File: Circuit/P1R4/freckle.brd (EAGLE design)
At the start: 57.9 x 57.9 mm, 81 parts, among them J1 1981584-1, U1 MK20DX256VLH7, U2 TPS61200, U3 MPU-9250, U4 MINI54TAN, Y1 32.768KHz, Y2 16Mhz/8pF, Y3 26 Mhz, Y4 16 Mhz

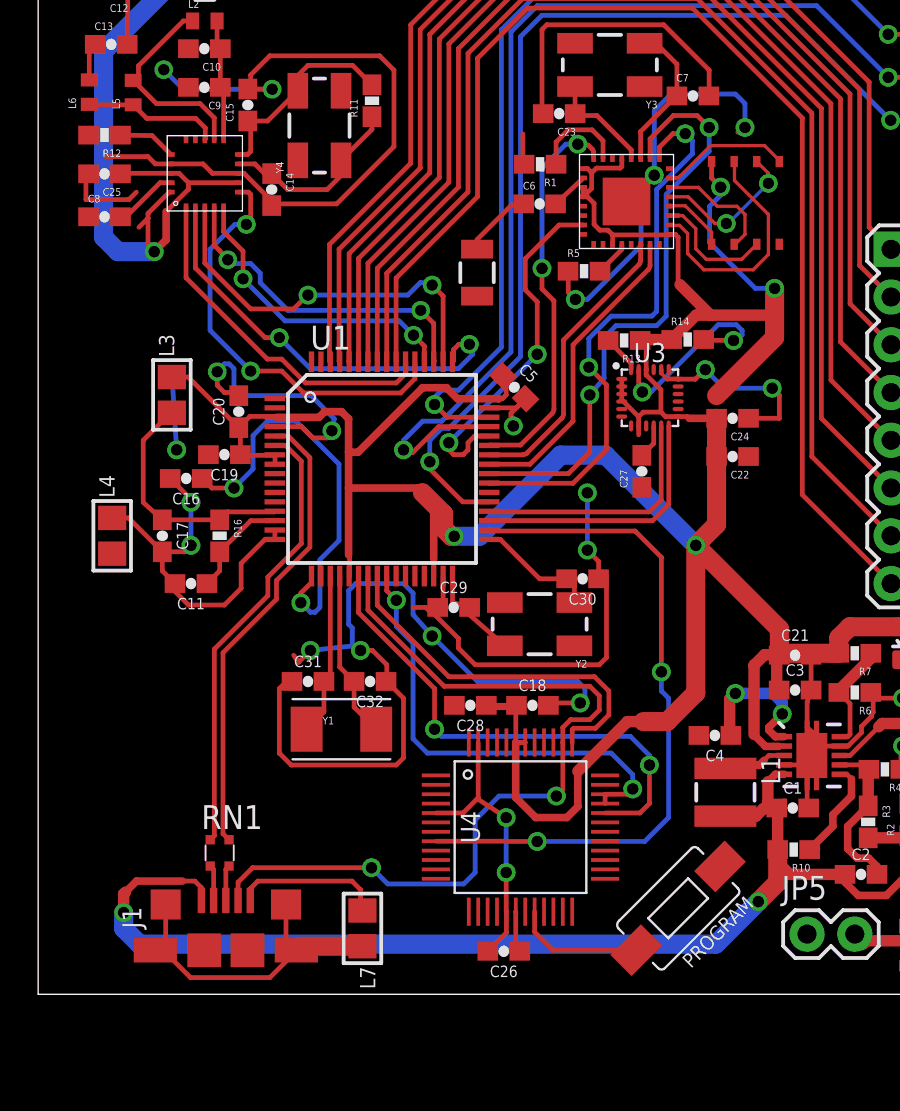
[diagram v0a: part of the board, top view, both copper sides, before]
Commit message: Generic R3_R4 minimum variant without code-loading capabilites and RGBs completed
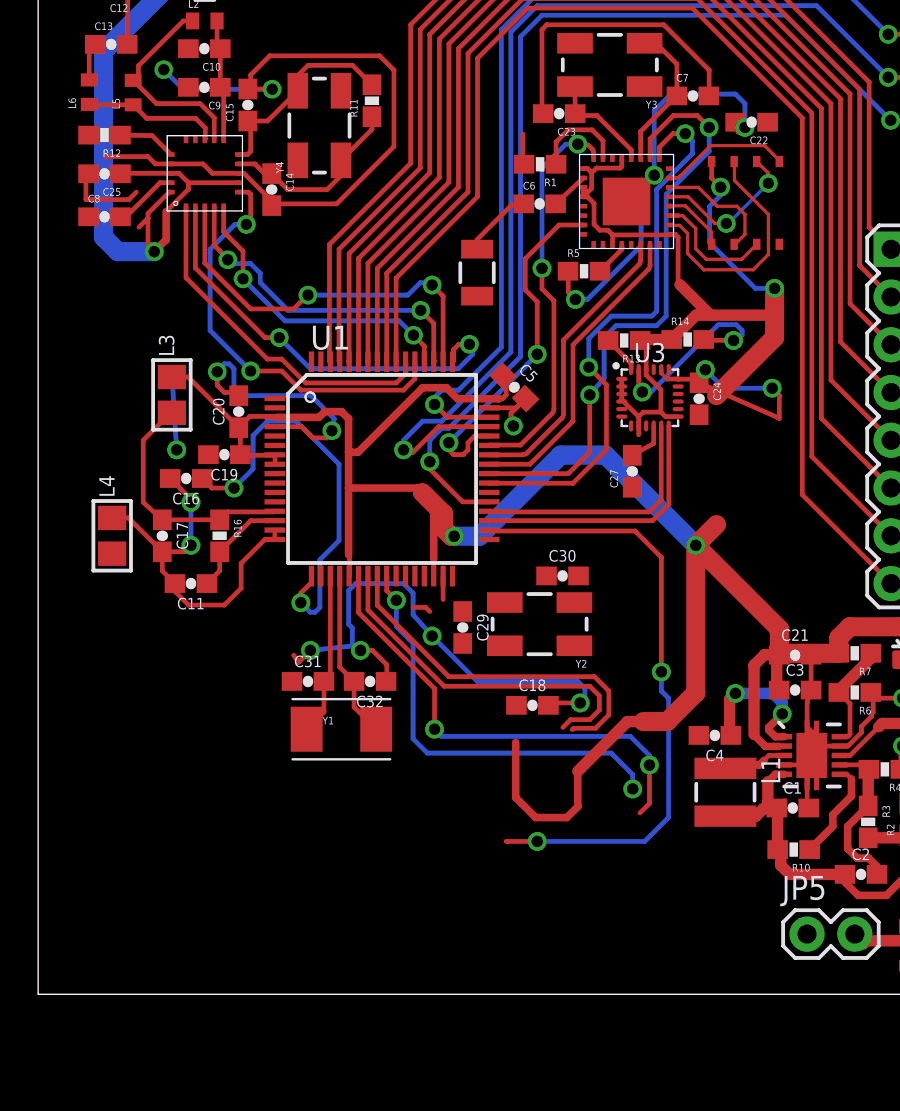
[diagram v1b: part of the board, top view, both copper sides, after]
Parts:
- removed C26, C28: 0.1uF, appfruits:0603-CAP
- removed J1: 1981584-1, con-usb:1981584-1
- removed L7: 600 Ohm/100 Mhz, appfruits:0805
- removed PROGRAM: Program, SparkFun-Electromechanical:TACTILE-SWITCH-1101NE
- removed RN1: 33, resistor-dil:EXB34V
- removed U4: MINI54TAN, TeensyCustom:MINI54TAN
- moved C22 17.8 mm to (37.9, 46.4)
- moved C24 2.06 mm to (35.2, 31.7), turned to 270 degrees
- moved C29 1.17 mm to (22.6, 19.5), turned to 270 degrees
- moved C30 1.08 mm to (27.9, 22.3), turned to 0 degrees
- moved C27 0.51 mm to (31.6, 27.8)
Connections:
- removed net N$10: PROGRAM.P$2, U4.20
- removed net N$11: C26.1, U4.18
- removed net USB_CON_N: J1.2, RN1.1
- removed net USB_CON_P: J1.3, RN1.2
- removed net USB_SHIELD: J1.S1, J1.S2, J1.S3, J1.S4, L7.2
- net 3.3V: no longer C28.1, U4.42, U4.43
- net GND: no longer C26.2, C28.2, J1.5, L7.1, PROGRAM.P$1, U4.17, U4.25, U4.47, U4.5
- net ID: no longer J1.4, U4.38
- net PTA2: no longer U4.37
- net RESET_B: no longer U4.8
- net SWD_CLK: no longer U4.32
- net SWD_DIO: no longer U4.33, U4.34
- net USB_D_N: no longer RN1.4
- net USB_D_P: no longer RN1.3
- net VCC: no longer J1.1
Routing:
- net VCC: track 76.6 -> 29.9 mm, vias 2 -> 0
- net GND: track 165.4 -> 139.0 mm, vias 21 -> 17
- net ID: track 45.0 -> 19.1 mm, vias 2 -> 0
- net USB_D_P: track 24.7 -> 0.00 mm
- net USB_D_N: track 23.9 -> 0.00 mm
- net USB_SHIELD: track 17.8 -> 0.00 mm
- net 3.3V: track 293.4 -> 276.3 mm
- net N$31: track 15.8 -> 0.00 mm
- net N$15: track 15.1 -> 0.00 mm
- net N$10: track 6.88 -> 0.00 mm
- net N$28: track 6.77 -> 0.00 mm
- net N$27: track 5.36 -> 0.00 mm
- net RESET_B: track 36.7 -> 32.9 mm
- net N$11: track 2.58 -> 0.00 mm
- net USB_CON_N: track 1.90 -> 0.00 mm
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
